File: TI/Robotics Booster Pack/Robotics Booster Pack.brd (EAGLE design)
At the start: 71.1 x 67.3 mm, 92 parts, among them U1 TPS62177.DQC, U11 SCHA4B0400, U13 XBEE-1XBEE-1_LOCK, U14 TPS5450, U3 DRV8800, U4 DRV8800, U5 DRV8800, U6 DRV8800, U7 PCA9557.RGV, U8 MPU-6050, U9 INA220.DGS

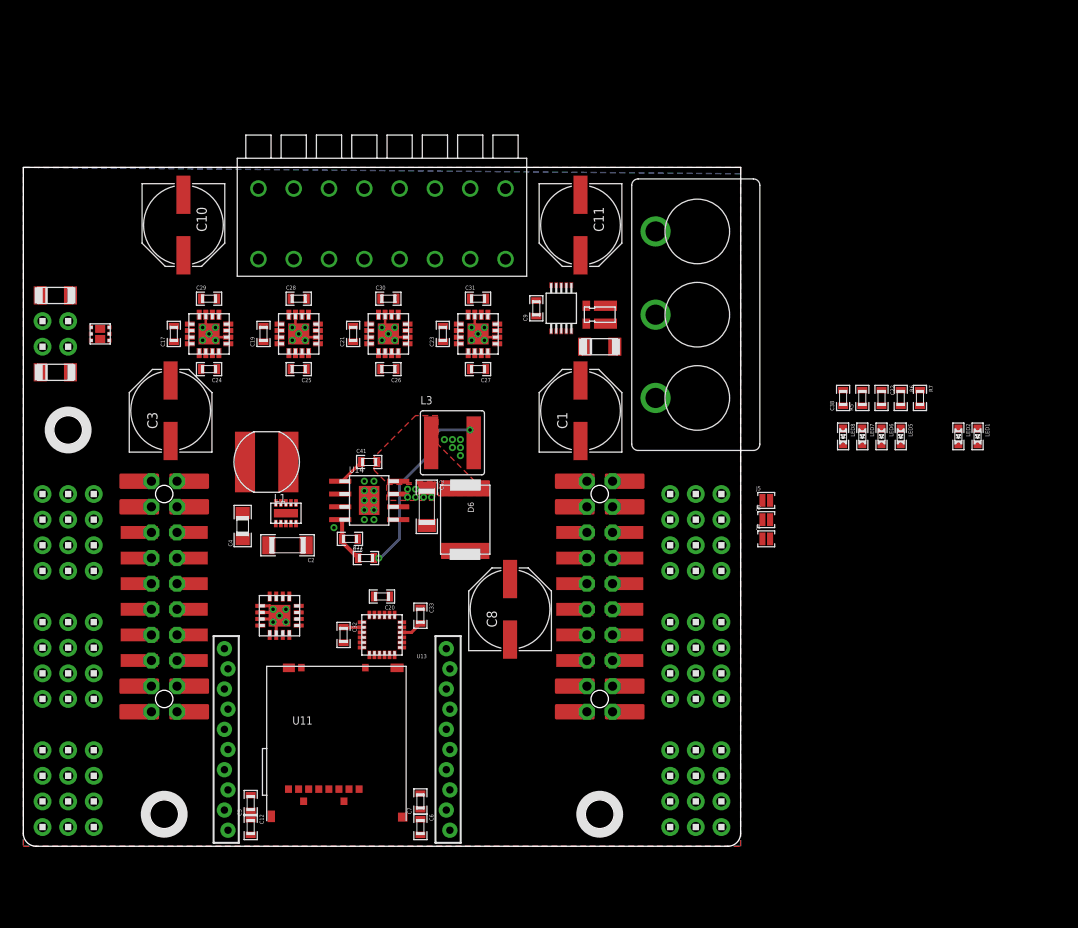
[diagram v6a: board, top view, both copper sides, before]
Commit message: Part placement ~90% completed. Started routing. Pin mapping figured out (for the most part).
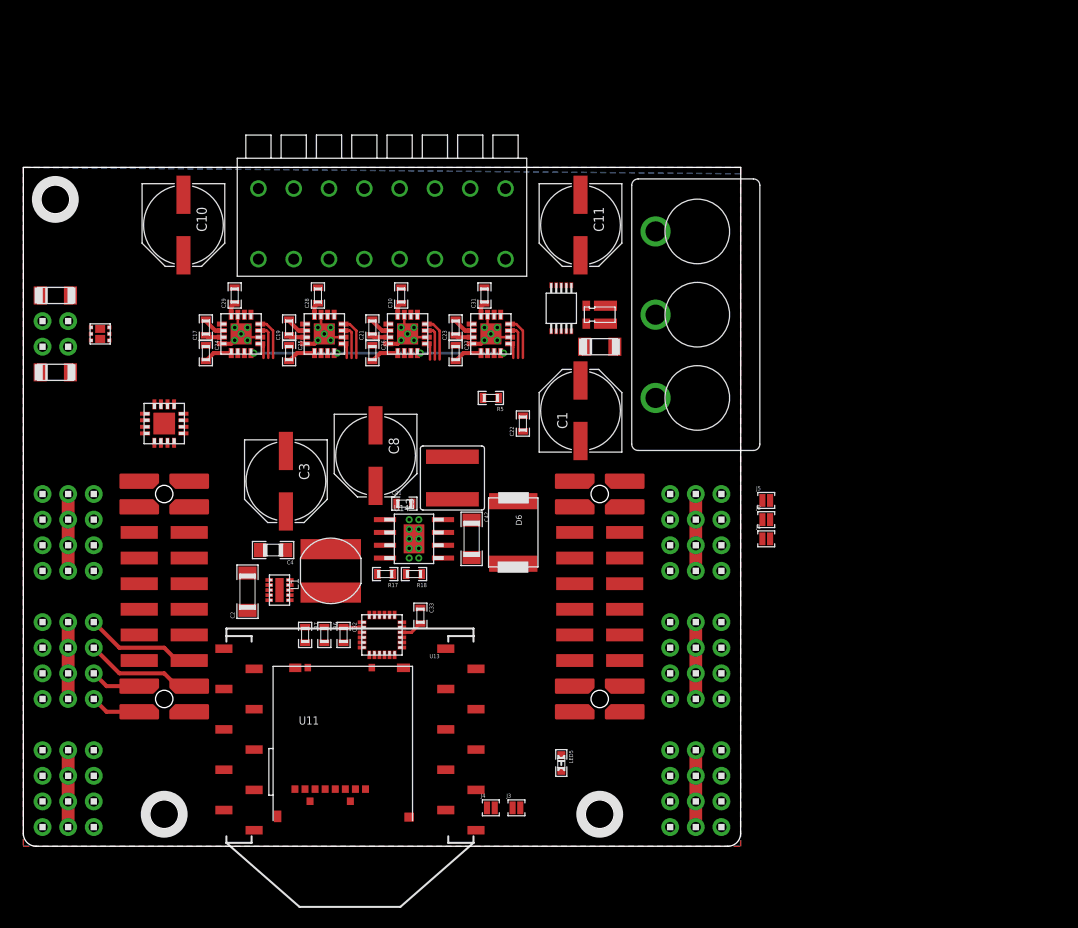
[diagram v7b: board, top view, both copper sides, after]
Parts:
- removed C12, C20, C38, C6, C9: .1uF, standardparts:0603
- removed C5, C7: 1uF, standardparts:0603
- removed LED1, LED2, LED6, LED7, LED8: (no value), standardparts:0603.LED
- removed U$8: STELLARIS-LAUNCHPADSTELLARIS-LAUNCHPAD-XL, StellarisLaunchPad_Fred:LAUNCHPAD-XL
- removed U7: PCA9557.RGV, packages(ti):RGV.16
- added J3, J4: (no value), solderjumper:2.LRG
- added U2: PCA9538.RGV, packages(ti):RGV.16
- U13: value XBEE-1XBEE-1_LOCK -> XBEE-1B3; device SparkFun-RF:XBEE-1_LOCK -> SparkFun-RF:XBEE-SMD
- moved R7 65.3 mm to (27.9, 21.0)
- moved R6 61.8 mm to (29.8, 21.0)
- moved LED5 46.7 mm to (53.3, 8.26)
- moved R5 36.8 mm to (46.4, 44.5), turned to 180 degrees
- moved C22 35.7 mm to (49.5, 41.9), turned to 90 degrees
- moved U$21 22.9 mm to (3.17, 64.1)
- moved C8 20.3 mm to (34.9, 38.7), turned to 270 degrees
- moved C3 13.4 mm to (26.0, 36.2), turned to 270 degrees
- moved L1 12.5 mm to (30.5, 27.3), turned to 90 degrees
- moved U1 7.65 mm to (25.4, 25.4), turned to 0 degrees
- moved R18 7.25 mm to (38.7, 27.0)
- moved C2 6.08 mm to (22.2, 25.2), turned to 90 degrees
- moved U14 5.85 mm to (38.7, 30.5)
- moved C42 5.46 mm to (44.5, 30.5)
- moved C41 5.41 mm to (37.8, 34.0)
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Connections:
- removed net AD0: U$8.PD2
- removed net AD1: U$8.PD3
- removed net AD2: U$8.PE0
- removed net AD3: U$8.PE1
- removed net AD4: U$8.PE2
- removed net AD5: U$8.PE3
- removed net I2C.SCL: R6.2, U$8.PB2, U7.15, U8.23, U9.5
- removed net I2C.SDA: R7.2, U$8.PB3, U7.16, U8.24, U9.4
- removed net M0.DIR: U$8.PC4, U5.1
- removed net M0.SPD: U$8.PA7, U5.4
- removed net M1.DIR: U$8.PC7, U6.1
- removed net M1.SPD: U$8.PA6, U6.4
- removed net M2.DIR: U$8.PF0, U3.1
- removed net M2.SPD: U$8.PD1, U3.4
- removed net M3.DIR: U$8.PF4, U4.1
- removed net M3.SPD: U$8.PD0, U4.4
- removed net N$10: LED2.P$1
- removed net N$11: LED1.P$1
- removed net N$14: LED8.P$2
- removed net N$5: LED1.P$2
- removed net N$8: LED2.P$2
- removed net N$9: LED7.P$2
- removed net QEI0.A: U$8.PD6
- removed net QEI0.B: U$8.PD7
- removed net QEI1.A: U$8.PC5
- removed net QEI1.B: U$8.PC6
- removed net SPI.!CS: U$8.PA3, U11.!CS!/NC/DAT3
- removed net SPI.MISO: U$8.PA4, U11.MISO/DAT0
- removed net SPI.MOSI: U$8.PA5, U11.MOSI/CMD
- removed net SPI.SCLK: U$8.PA2, U11.CLK
- removed net SVRO0: U$8.PB6
- removed net SVRO1: U$8.PB7
- removed net SVRO2: U$8.PB4
- removed net SVRO3: U$8.PB5
- removed net SVRO4: U$8.PE4
- removed net SVRO5: U$8.PE5
- removed net UART1.RXI: U$8.PB0
- removed net UART1.TXO: U$8.PB1
- net !RST: now also U2.1; no longer U$8.RST, U7.13
- net 3.3V: now also C3.+, U2.14; no longer C12.1, C20.1, C38.1, C5.1, C6.1, C7.1, C9.1, U$8.3.3V, U7.14
- net 5.0V: no longer U$8.VBUS
- net FET0.G: now also U2.9; no longer U7.7
- net FET1.G: now also U2.10; no longer U7.8
- net GND: now also C3.-, U2.15, U2.16, U2.6, U2.PAD; no longer C12.2, C20.2, C38.2, C5.2, C6.2, C7.2, C9.2, U$8.GND1, U$8.GND2, U7.1, U7.2, U7.3, U7.6, U7.PAD
- net IMU.INT: now also U2.8; no longer U7.5
- net M0.EN: now also U2.5; no longer U7.9
- net M1.EN: now also U2.4; no longer U7.10
- net M2.EN: now also U2.3; no longer U7.11
- net M3.EN: now also U2.2; no longer U7.12
- net PA2: now also U11.!CS!/NC/DAT3
- net PA3: now also U11.CLK
- net PA4: now also U11.MISO/DAT0
- net PA5: now also U11.MOSI/CMD
- net PA6: now also U6.4
- net PA7: now also U5.4
- net PB0: now also J3.1
- net PB1: now also J4.1
- net PB2: now also R6.2, U2.12, U8.23, U9.5
- net PB3: now also R7.2, U2.13, U8.24, U9.4
- net PC4: now also U5.1
- net PC7: now also U3.1
- net PD0: now also U4.4
- net PD1: now also U3.4
- net PD2: now also H1.1, U2.11; no longer H4.2
- net PD3: now also H1.2; no longer H4.1
- net PE0: now also H1.3; no longer H1.4
- net PE1: now also H1.4; no longer H1.3
- net PE2: now also H4.1; no longer H1.2
- net PE3: now also H4.2; no longer H1.1
- net PF0: now also U6.1
- net PF3: now also U4.1
- net XBEE.ASSOCIATE: no longer LED6.P$1
- net XBEE.CONNECTED: now also U2.7; no longer U7.4
- net XBEE.RSSI: no longer LED5.P$1
- net XBEE.RXI: now also J3.2
- net XBEE.TXO: now also J4.2
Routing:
- net M.MODE: track 0.00 -> 26.0 mm, vias 0 -> 4
- net 5.0V: track 20.2 -> 0.00 mm, vias 2 -> 0
- net PE2: track 0.00 -> 11.0 mm
- net PE3: track 0.00 -> 11.0 mm
- net PA7: track 0.00 -> 9.28 mm
- net PA6: track 0.00 -> 9.28 mm
- net N$70: track 0.00 -> 7.62 mm
- net N$67: track 0.00 -> 7.62 mm
- net N$71: track 0.00 -> 7.62 mm
- net N$68: track 0.00 -> 7.62 mm
- net N$69: track 0.00 -> 7.62 mm
- net N$66: track 0.00 -> 7.62 mm
- net N$35: track 4.71 -> 0.16 mm
- net PD1: track 0.00 -> 4.40 mm
- net PD0: track 0.00 -> 4.25 mm
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- removed copper zone on layer 1, net N$34
- removed copper zone on layer 1, net VBAT

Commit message: Part placement is mostly complete for RBP v3. Layout coming along. Routing multiple Power Header Options will be difficult...
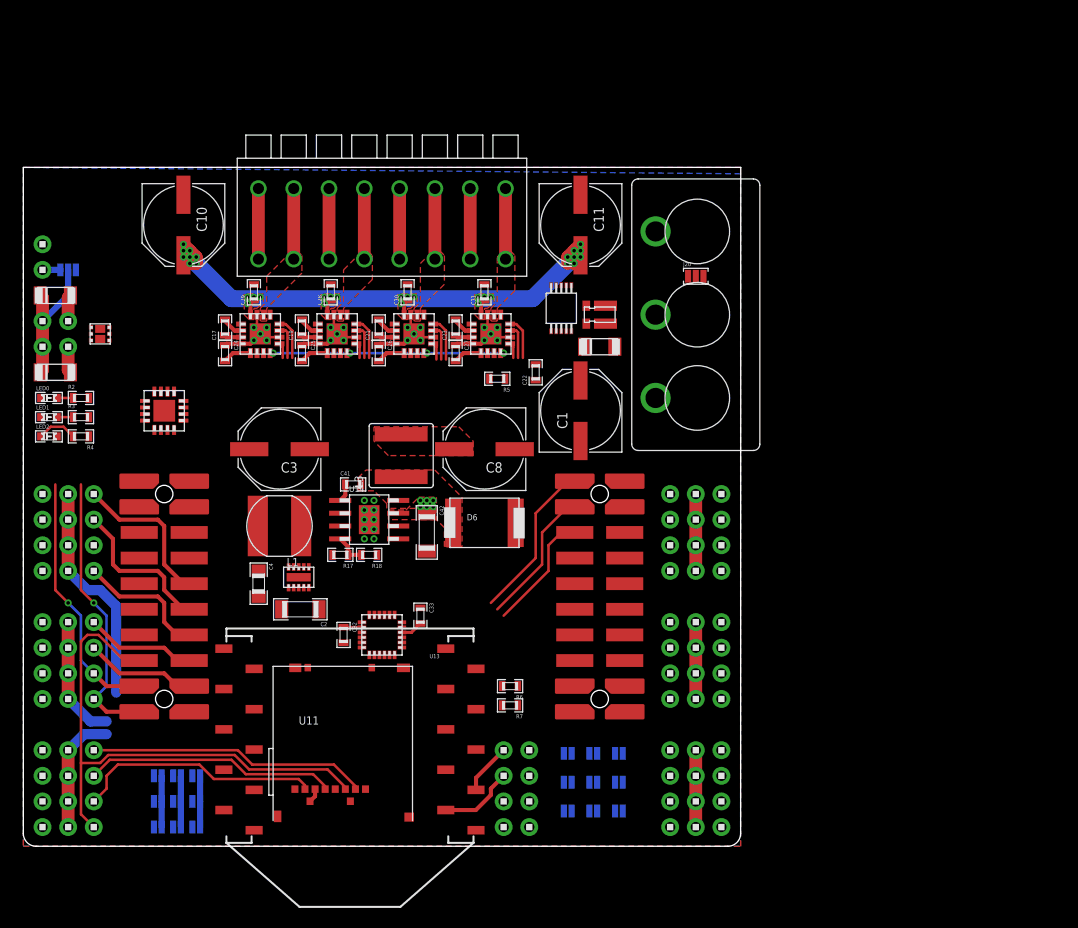
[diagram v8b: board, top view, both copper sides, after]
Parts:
- removed LED5: (no value), standardparts:0603.LED
- removed U$21, U$3, U$4: HOLE.4MM, screw_holes:4MM
- added H21, H22: 1X4, headers(.1in):1X4
- added H23: 1X2, headers(.1in):1X2
- added J10, J11, J12, J13, J14, J15, J16, J17, J18, J19, J6, J7, J8, J9: (no value), solderjumper:2.LRG
- added J20: (no value), solderjumper:3.LRG.12
- added LED0, LED1, LED2: (no value), standardparts:0603.LED
- added R2, R4: 1k, standardparts:0603
- added R3: 1.5k, standardparts:0603
- J5: device solderjumper:2.LRG -> solderjumper:3.LRG
- moved J5 72.9 mm to (4.45, 57.1), flipped to the bottom
- moved J1 64.7 mm to (13.3, 6.99), flipped to the bottom
- moved J2 63.7 mm to (15.2, 6.99), flipped to the bottom
- moved J4 33.0 mm to (13.3, 4.45), flipped to the bottom
- moved J3 31.9 mm to (17.1, 6.99), flipped to the bottom
- moved R7 21.5 mm to (48.3, 14.0), turned to 180 degrees
- moved R6 19.1 mm to (48.3, 15.9), turned to 180 degrees
- moved C8 10.8 mm to (45.7, 39.4), turned to 180 degrees
- moved L1 6.75 mm to (25.4, 31.8), turned to 180 degrees
- moved L3 5.54 mm to (37.5, 38.7)
- moved C2 5.52 mm to (27.5, 23.5), turned to 180 degrees
- moved C41 5.43 mm to (32.7, 35.9)
- moved C22 5.24 mm to (50.8, 47.0)
- moved R18 4.84 mm to (34.3, 28.9)
- moved U14 4.84 mm to (34.3, 32.4)
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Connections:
- removed net N$66: H11.1, H11.2, H11.3, H11.4
- removed net N$67: H14.1, H14.2, H14.3, H14.4
- removed net N$68: H17.1, H17.2, H17.3, H17.4
- removed net N$69: H2.1, H2.2, H2.3, H2.4
- removed net N$70: H5.1, H5.2, H5.3, H5.4
- removed net N$71: H8.1, H8.2, H8.3, H8.4
- removed net N$72: C10.+, C28.1, C29.1, U5.8, U6.8
- removed net N$73: C11.+, C30.1, C31.1, U3.8, U4.8
- removed net XBEE.ASSOCIATE: U13.15
- removed net XBEE.RSSI: U13.6
- removed net XBEE.RXI: J3.2, U13.2
- removed net XBEE.TXO: J4.2, U13.3
- new net N$2: LED0.P$2, R2.1
- new net N$3: LED1.P$2, R3.1
- new net N$4: R4.1, U13.13
- new net N$5: H23.1, J5.3
- new net V1: H2.1, H2.2, H2.3, H2.4, J1.2, J2.2, J3.2
- new net V2: H5.1, H5.2, H5.3, H5.4, J4.2, J6.2, J7.2
- new net V3: H8.1, H8.2, H8.3, H8.4, J10.2, J8.2, J9.2
- new net V4: H11.1, H11.2, H11.3, H11.4, J11.2, J12.2, J13.2
- new net V5: H14.1, H14.2, H14.3, H14.4, J14.2, J15.2, J16.2
- new net V6: H17.1, H17.2, H17.3, H17.4, J17.2, J18.2, J19.2
- new net VMOTOR: C10.+, C11.+, C28.1, C29.1, C30.1, C31.1, J20.2, U3.8, U4.8, U5.8, U6.8
- net 3.3V: now also H21.1, H22.1, J10.1, J13.1, J16.1, J19.1, J3.1, J7.1, LED0.P$1
- net 5.0V: now also J12.1, J15.1, J18.1, J2.1, J20.3, J6.1, J9.1, LED1.P$1
- net GND: now also H21.2, H22.2, H23.2, LED2.P$2, R2.2, R3.2
- net PB0: now also H21.3, U13.2; no longer J3.1
- net PB1: now also H21.4, U13.3; no longer J4.1
- net PB2: now also H22.4
- net PB3: now also H22.3
- net VBAT: now also J1.1, J11.1, J14.1, J17.1, J20.1, J4.1, J5.1, J8.1
- net VFET: now also J5.2
- net XBEE.CONNECTED: now also LED2.P$1, R4.2; no longer U13.17
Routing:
- net VMOTOR: track 0.00 -> 85.9 mm, vias 0 -> 32
- net PA5: track 0.00 -> 54.1 mm
- net PA2: track 0.00 -> 43.6 mm
- net PA3: track 0.00 -> 38.7 mm
- net PA4: track 0.00 -> 36.4 mm
- net PA7: track 9.28 -> 32.1 mm, vias 0 -> 1
- net V1: track 0.00 -> 22.4 mm
- net PA6: track 9.28 -> 29.6 mm, vias 0 -> 1
- net PD3: track 0.00 -> 15.4 mm
- net PD2: track 0.00 -> 15.4 mm
- net VFET: track 0.00 -> 13.9 mm
- net PE1: track 0.00 -> 13.2 mm
- net V2: track 0.00 -> 12.4 mm
- net V3: track 0.00 -> 12.1 mm
- net GND: track 25.5 -> 33.5 mm
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- added copper zone on layer 1, net 5.0V
- added copper zone on layer 1, net M0-
- added copper zone on layer 1, net M1-
- added copper zone on layer 1, net M2-
- added copper zone on layer 1, net M3-
- added copper zone on layer 1, net N$34
- added copper zone on layer 1, net VBAT
- added copper zone on layer 1, net VMOTOR
- added copper zone on layer 16, net VMOTOR
